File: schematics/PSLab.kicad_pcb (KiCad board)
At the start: 4 copper layers, 99 x 53.3 mm, 169 parts, among them CON1 USB-MINI-B, J1 Programmer, J10 GND, J11 Vbus, J12 SD_Switch, J13 D+, J14 D-, J16 I2C-2, J2 DoublePins, J3 LA, J4 Outputs, J5 Bluetooth, J6 I2C-1, J7 UART/ESP, J8 Power Pins, J9 SPI, P1 SDCard, Q1 MMBT3906, Q2 MMBT3904, Q3 MMBT3906, U1 LDFM33PVR, U10 TL082, U11 6S21, U12 6S21, U13 TL082, U14 CP2102, U15 ESP8266, U16 TL082, U17 SP0503BAHT, U2 74HC126, U3 PIC24EP256GP204, U4 TC1240A, U5 7660, U7 LM324, U8 TL082, U9 MCP4728, X1 12MHz

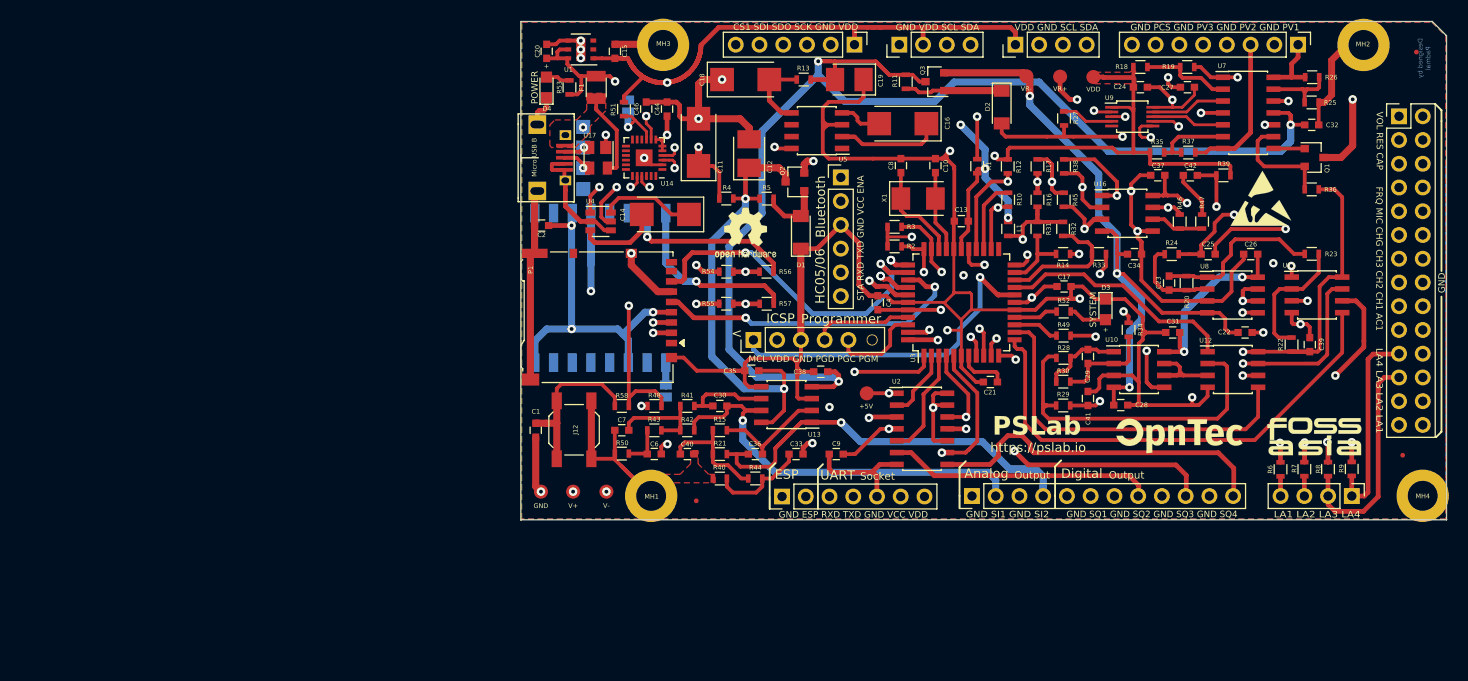
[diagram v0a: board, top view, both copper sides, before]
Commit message: feat: added components for RTC
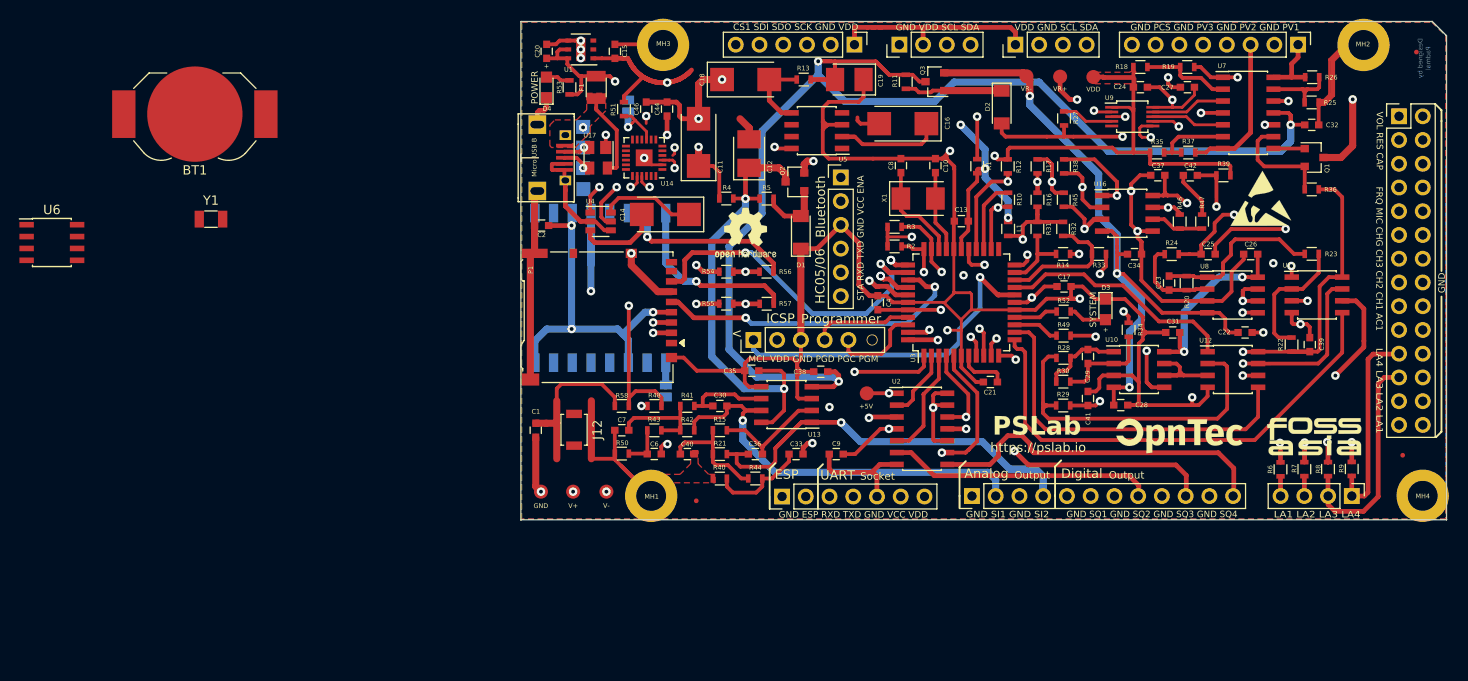
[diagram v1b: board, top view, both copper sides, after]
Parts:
- added BT1: 1225, Battery:BatteryHolder_LINX_BAT-HLD-012-SMT, F.Cu at (56.1, 70.2)
- added TP11: CR1225, Battery:Battery_CR1225, F.Cu at (62.1, 73.9)
- added U6: DS1307Z+, Package_SO:SOIC-8_3.9x4.9mm_P1.27mm, F.Cu at (40.8, 83.9)
- added Y1: 32.768 kHz, Crystal:Crystal_SMD_3215-2Pin_3.2x1.5mm, F.Cu at (57.8, 81.4)
- C1: value 1n -> 1nF
- J12: footprint Buttons_Switches_SMD:SW_SPST_SKQG -> Button_Switch_SMD:SW_SPST_B3U-1000P
- R51: value 1k -> 1K
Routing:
- net 3.3V: track 286.2 -> 263.5 mm
- net GND: track 462.7 -> 449.0 mm
- net VBus: track 19.6 -> 17.6 mm
- net Net-(C16-Pad2): track 4.65 -> 2.80 mm
- net D-: track 14.6 -> 13.5 mm

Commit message: route: adding missing routes after importing net
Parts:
- removed J3: LA, Pin_Headers:Pin_Header_Straight_1x04_Pitch2.54mm
- removed REF***: OSHW-Logo_5.7x6mm_SilkScreen, Symbols:OSHW-Logo_5.7x6mm_SilkScreen
- moved BT1 40.2 mm to (63.8, 109.6)
- moved U6 30.7 mm to (66.4, 100.7)
- moved Y1 18.3 mm to (60.6, 99.5), turned to 90 degrees
- moved S6 6.40 mm to (176.6, 98.3)
- moved R6 4.98 mm to (172.3, 103.2), turned to 270 degrees
- moved R8 4.96 mm to (177.1, 103.2), turned to 270 degrees
- moved R7 4.96 mm to (174.6, 103.2), turned to 270 degrees
- moved R9 4.94 mm to (179.8, 103.2), turned to 270 degrees
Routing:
- net IDC: track 24.4 -> 0.07 mm
- net 3.3V: track 263.5 -> 287.7 mm
- net IDA: track 23.8 -> 0.02 mm
- net IDD: track 22.0 -> 0.08 mm
- net IDB: track 20.7 -> 0.04 mm
- net /ID2: track 50.6 -> 46.4 mm
- net /ID3: track 47.7 -> 45.5 mm
- net /ID4: track 46.2 -> 44.1 mm
- net /ID1: track 45.2 -> 43.2 mm
- net VBus: track 17.6 -> 19.6 mm
- net CS.CH1: track 52.5 -> 54.2 mm
- net D-: track 13.5 -> 14.6 mm
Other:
- board text removed: "LA 1"
- board text removed: "LA 2"
- board text removed: "LA 3"
- board text removed: "LA 4"
- board text removed: "LA1 LA2 LA3 LA4"

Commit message: route: rearrange to get more space
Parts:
- moved TP11 117.1 mm to (174.3, 107.3)
- moved BT1 110.5 mm to (174.3, 107.3)
- moved U6 98.1 mm to (162.5, 120.3)
- moved Y1 93.8 mm to (150.3, 127.1)
- moved S6 93.7 mm to (83.6, 109.6)
- moved R9 7.45 mm to (181.1, 95.8), turned to 180 degrees
- moved R36 6.82 mm to (181.1, 82.3)
- moved R8 6.21 mm to (181.1, 98.4), turned to 180 degrees
- moved Q1 6.16 mm to (180.9, 78.3)
- moved C1 6.12 mm to (98.1, 101.4), turned to 0 degrees
- moved R7 5.53 mm to (177.3, 98.4), turned to 180 degrees
- moved R23 5.50 mm to (181.1, 85.2)
- moved R6 5.00 mm to (173.7, 98.4), turned to 180 degrees
- moved C36 4.55 mm to (112.2, 104.0)
- moved J7 3.81 mm to (115.1, 111.1)
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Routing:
- net GND: track 449.0 -> 480.4 mm, vias 20 -> 25
- net Net-(Q1-Pad2): track 11.7 -> 25.7 mm
- net IDA: track 0.02 -> 13.4 mm
- net SINE2: track 51.6 -> 40.4 mm
- net IDB: track 0.04 -> 8.39 mm
- net SQR4: track 37.4 -> 29.6 mm, vias 0 -> 1
- net RxD: track 62.9 -> 55.6 mm
- net Net-(C1-Pad1): track 17.7 -> 10.9 mm
- net Net-(Q1-Pad1): track 3.37 -> 9.68 mm
- net IDD: track 0.08 -> 6.28 mm
- net IDC: track 0.07 -> 6.11 mm
- net /ID1: track 43.2 -> 49.0 mm
- net Net-(C23-Pad1): track 18.3 -> 23.8 mm
- net CS.CH1: track 54.2 -> 59.5 mm, vias 0 -> 2
- net /ID3: track 45.5 -> 50.8 mm
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
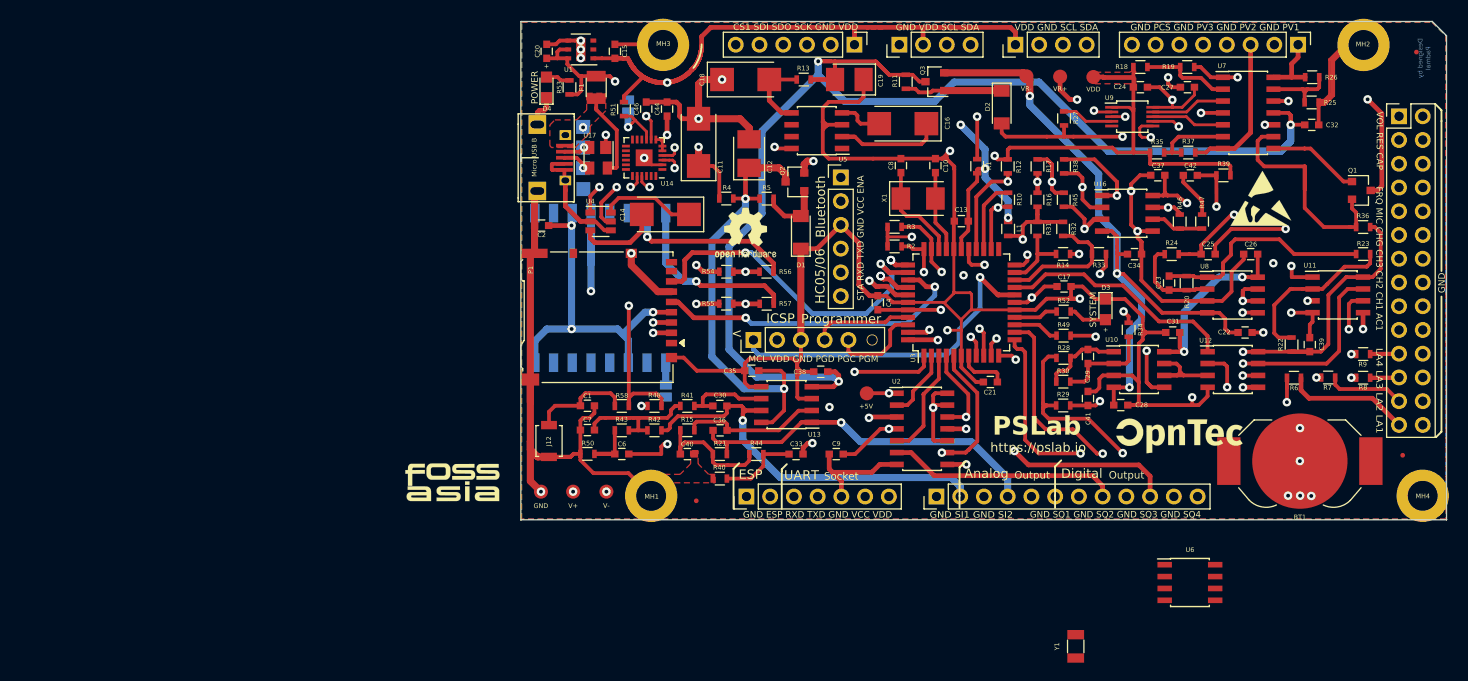
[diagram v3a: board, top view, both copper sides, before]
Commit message: route: rtc module placement
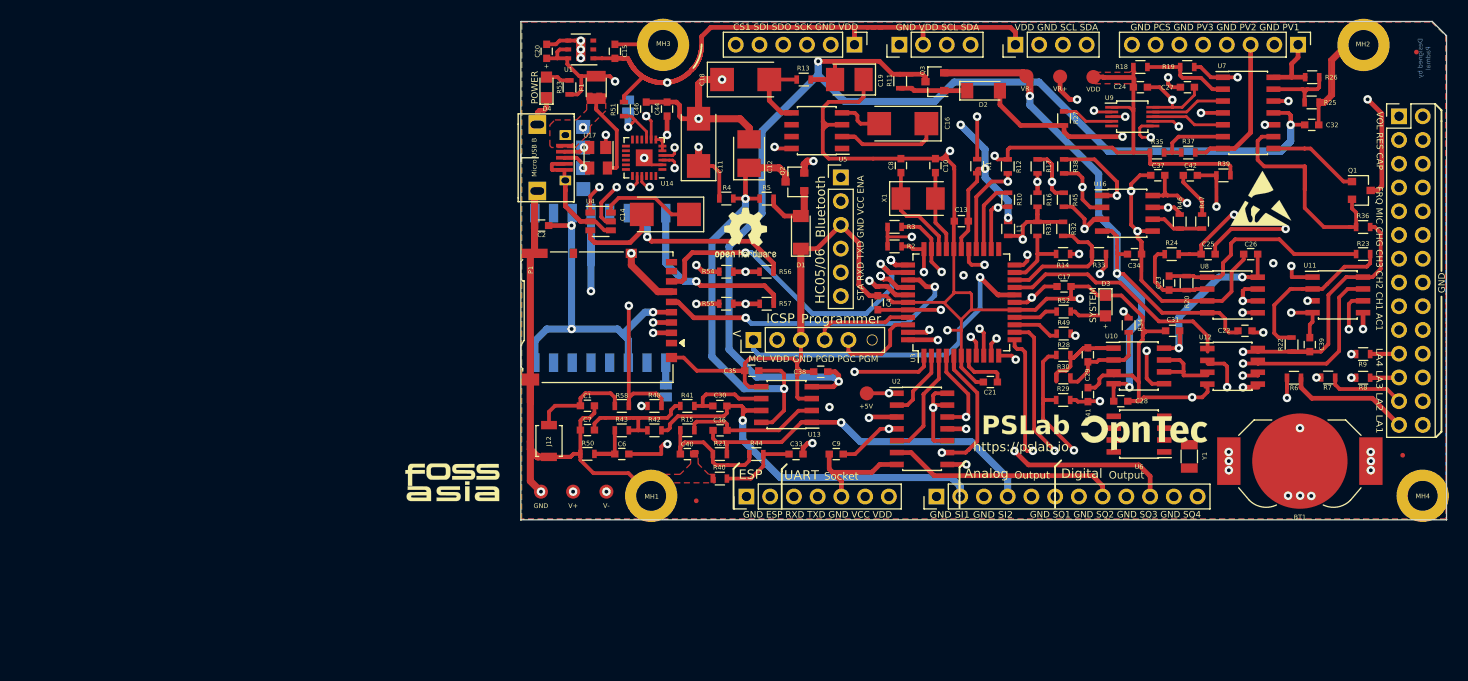
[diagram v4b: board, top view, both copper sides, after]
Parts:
- moved Y1 23.7 mm to (162.4, 106.8), turned to 270 degrees
- moved U6 16.8 mm to (157.1, 104.4), turned to 180 degrees
- moved S8 3.79 mm to (157.6, 104.3)
- moved D2 2.61 mm to (140.4, 67.7), turned to 0 degrees
- moved S2 1.18 mm to (145.0, 103.4)
- moved R11 0.60 mm to (131.5, 66.7)
- moved R29 0.59 mm to (149.0, 100.8)
- moved R34 0.48 mm to (156.0, 92.8)
- moved R30 0.45 mm to (149.0, 98.3)
- moved C28 0.42 mm to (155.1, 100.9)
- moved C41 0.41 mm to (151.6, 100.2)
- moved D3 0.41 mm to (153.5, 90.7)
- moved U10 0.38 mm to (157.1, 97.1)
- moved U12 0.34 mm to (167.1, 97.2)
- moved R28 0.31 mm to (149.0, 96.0)
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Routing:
- net Net-(BT1-Pad1): track 0.00 -> 47.5 mm, vias 0 -> 6
- net Net-(D2-Pad1): track 15.0 -> 7.28 mm
- net Net-(C29-Pad1): track 9.00 -> 13.0 mm
- net VR+: track 109.6 -> 106.3 mm
- net Net-(U10-Pad6): track 9.72 -> 8.18 mm
- net GND: track 480.4 -> 479.1 mm, vias 25 -> 24
- net Net-(R16-Pad1): track 52.2 -> 51.0 mm
- net CS.CH2: track 41.3 -> 42.2 mm
- net V-: track 193.7 -> 194.6 mm
- net CS.CH1: track 59.5 -> 60.1 mm
